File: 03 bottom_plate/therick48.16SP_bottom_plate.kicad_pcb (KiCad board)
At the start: 2 copper layers, 310.5 x 76 mm, 89 parts, among them U1 HOLE, U10 HOLE, U11 HOLE, U12 HOLE, U13 HOLE, U14 HOLE, U15 HOLE, U16 HOLE, U17 HOLE, U18 HOLE, U19 HOLE, U2 HOLE, U20 HOLE, U21 HOLE, U22 HOLE, U23 HOLE, U24 HOLE, U25 HOLE, U26 HOLE, U27 HOLE, U28 HOLE, U29 HOLE, U3 HOLE, U30 HOLE, U31 HOLE, U32 HOLE, U33 HOLE, U34 HOLE, U35 HOLE, U36 HOLE, U37 HOLE, U38 HOLE, U39 HOLE, U4 HOLE, U40 HOLE, U41 HOLE, U42 HOLE, U43 HOLE, U44 HOLE, U45 HOLE, U46 HOLE, U47 HOLE, U48 HOLE, U49 HOLE, U5 HOLE, U50 HOLE, U51 HOLE, U52 HOLE, U53 HOLE, U54 HOLE, U55 HOLE, U56 HOLE, U57 HOLE, U58 HOLE, U59 HOLE, U6 HOLE, U60 HOLE, U61 HOLE, U62 HOLE, U63 HOLE, U64 HOLE, U65 HOLE, U66 HOLE, U67 HOLE, U68 HOLE, U69 HOLE, U7 HOLE, U70 HOLE, U8 HOLE, U9 HOLE

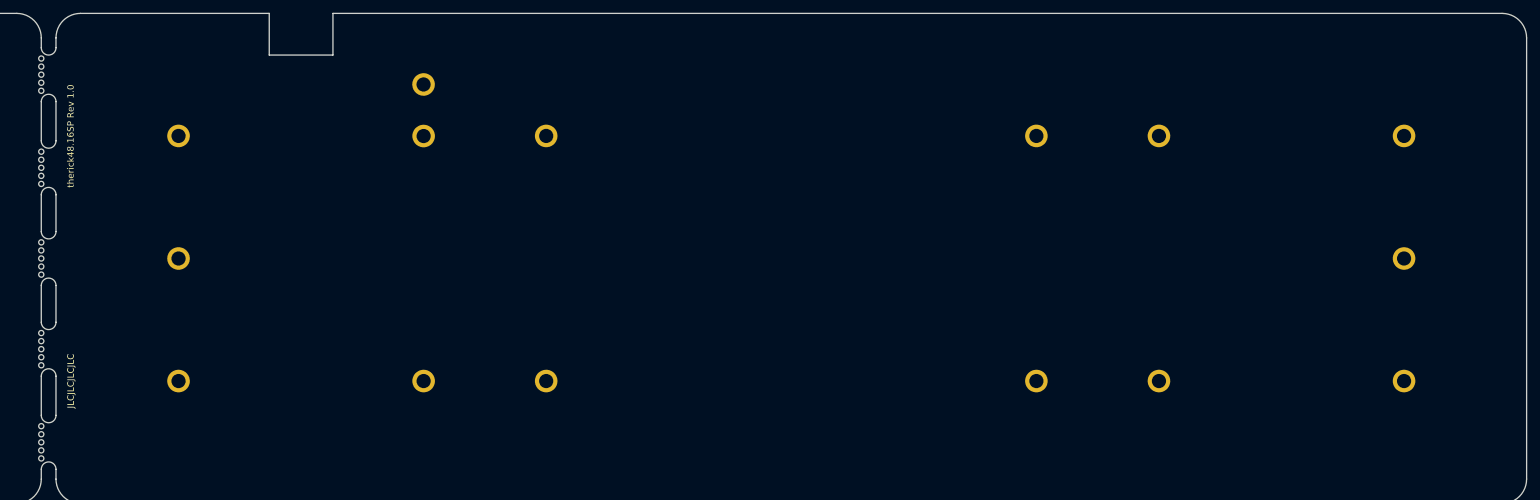
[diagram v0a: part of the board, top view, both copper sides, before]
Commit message: Made 2 columns able to be broken away
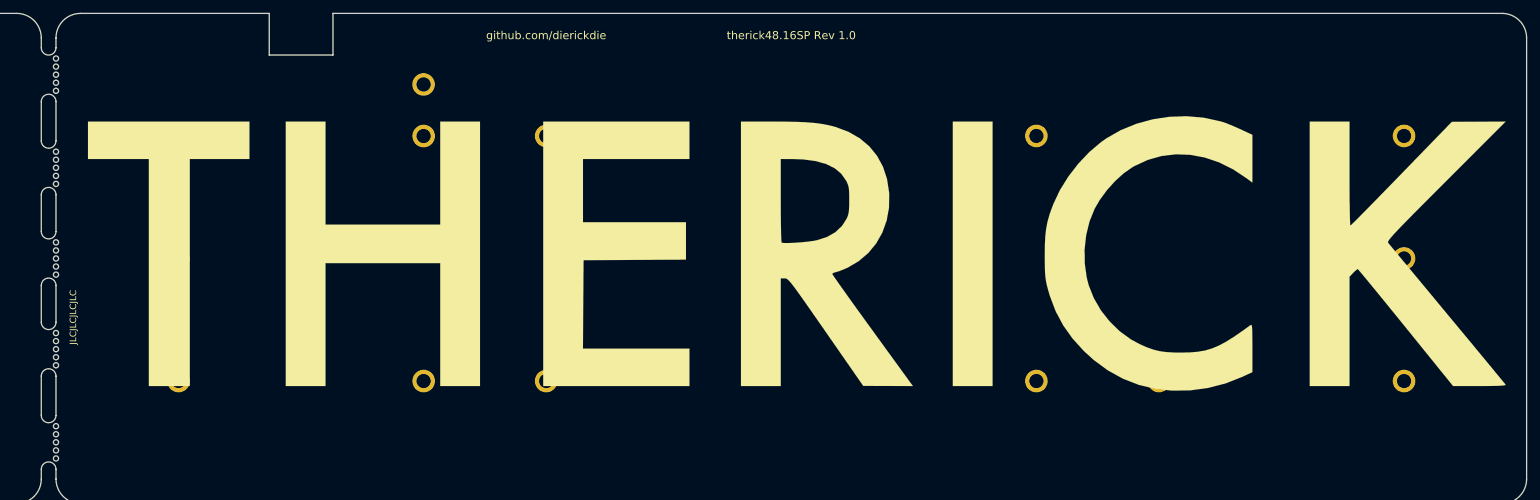
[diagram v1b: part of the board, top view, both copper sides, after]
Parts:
- added U71: HOLE, Artwork:THERICK, F.Cu at (259.9, 78.7)
- moved U66 2.28 mm to (145.9, 107.2)
- moved U67 2.28 mm to (145.9, 92.7)
- moved U68 2.28 mm to (145.9, 78.7)
- moved U69 2.28 mm to (145.9, 64.6)
- moved U70 2.28 mm to (145.9, 50.2)
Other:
- board text added: "github.com/dierickdie"

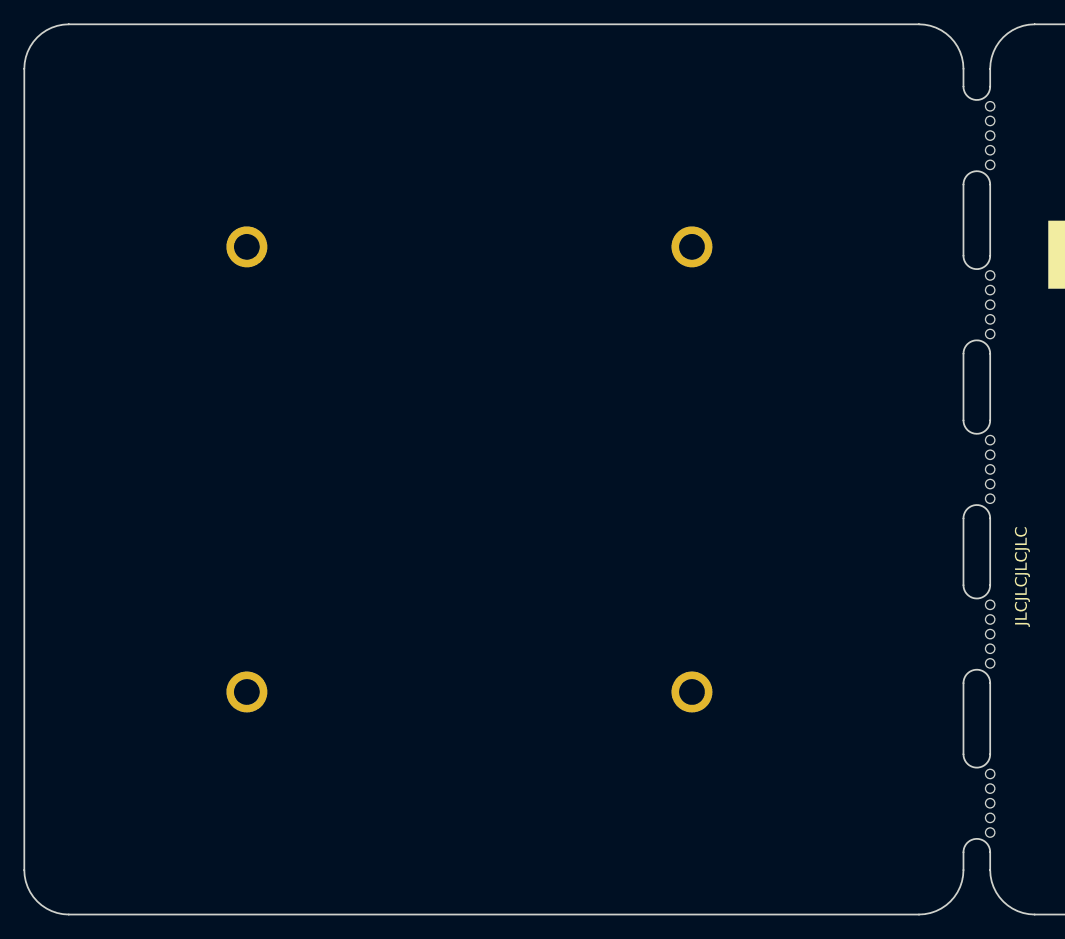
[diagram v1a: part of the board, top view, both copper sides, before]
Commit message: Added breakaway section, added rotary encoder support
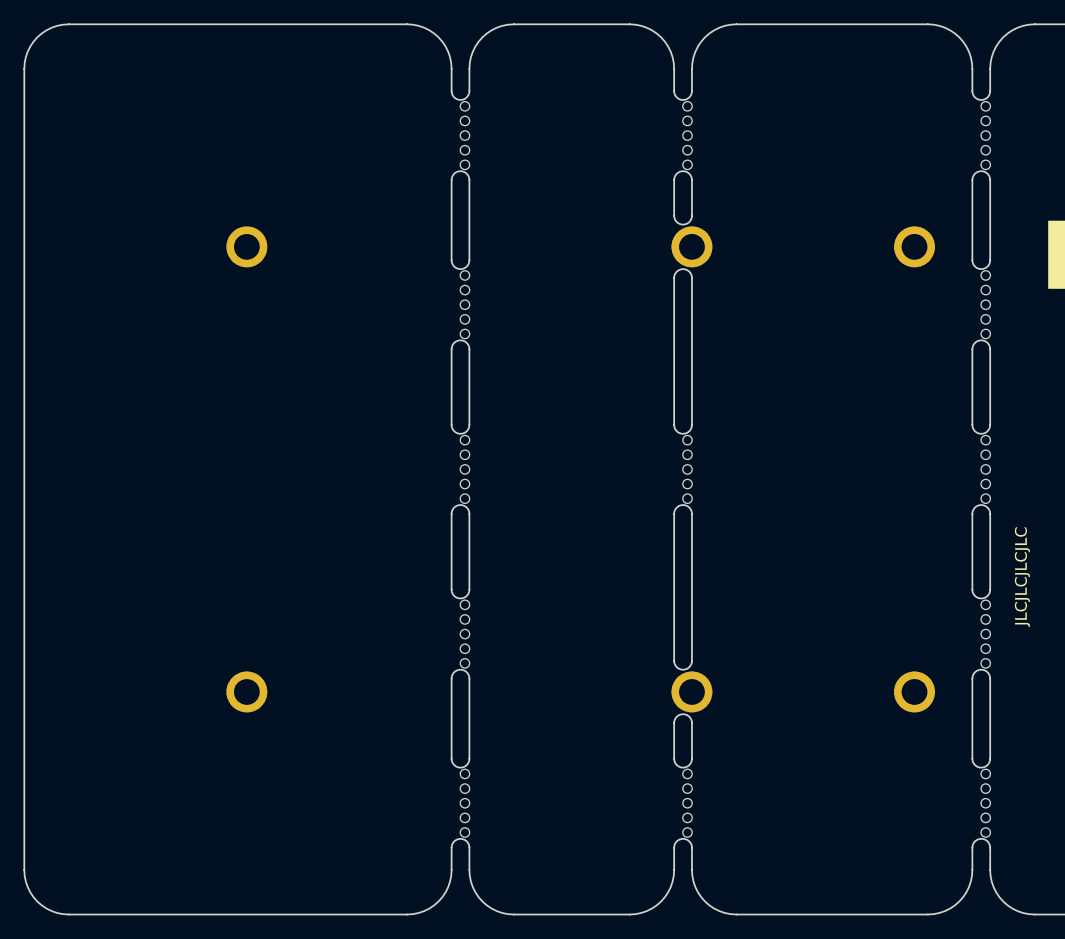
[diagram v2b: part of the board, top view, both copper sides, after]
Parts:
- added H20: MountingHole, random-keyboard-parts:Generic-Mounthole, F.Cu at (120.5, 97.7)
- added H21: MountingHole, random-keyboard-parts:Generic-Mounthole, F.Cu at (120.5, 59.7)
- added U72: HOLE, acheron_Hardware:MouseBite_IPC7351, F.Cu at (120.1, 107.2)
- added U73: HOLE, acheron_Hardware:MouseBite_IPC7351, F.Cu at (101.1, 64.6)
- added U74: HOLE, acheron_Hardware:MouseBite_IPC7351, F.Cu at (120.1, 50.2)
- added U75: HOLE, acheron_Hardware:MouseBite_IPC7351, F.Cu at (101.1, 78.7)
- added U76: HOLE, acheron_Hardware:MouseBite_IPC7351, F.Cu at (101.1, 50.2)
- added U77: HOLE, acheron_Hardware:MouseBite_IPC7351, F.Cu at (101.1, 107.2)
- added U78: HOLE, acheron_Hardware:MouseBite_IPC7351, F.Cu at (101.1, 92.7)
- added U79: HOLE, acheron_Hardware:MouseBite_IPC7351, F.Cu at (120.1, 78.7)
- moved H9 19.0 mm to (139.5, 97.7)
- moved H10 19.0 mm to (139.5, 59.7)
- moved U66 0.38 mm to (145.5, 107.2)
- moved U67 0.38 mm to (145.5, 92.7)
- moved U68 0.38 mm to (145.5, 78.7)
- moved U69 0.38 mm to (145.5, 64.6)
- moved U70 0.38 mm to (145.5, 50.2)
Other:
- outline, holes or cut-outs redrawn
